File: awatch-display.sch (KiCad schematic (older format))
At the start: 5 parts

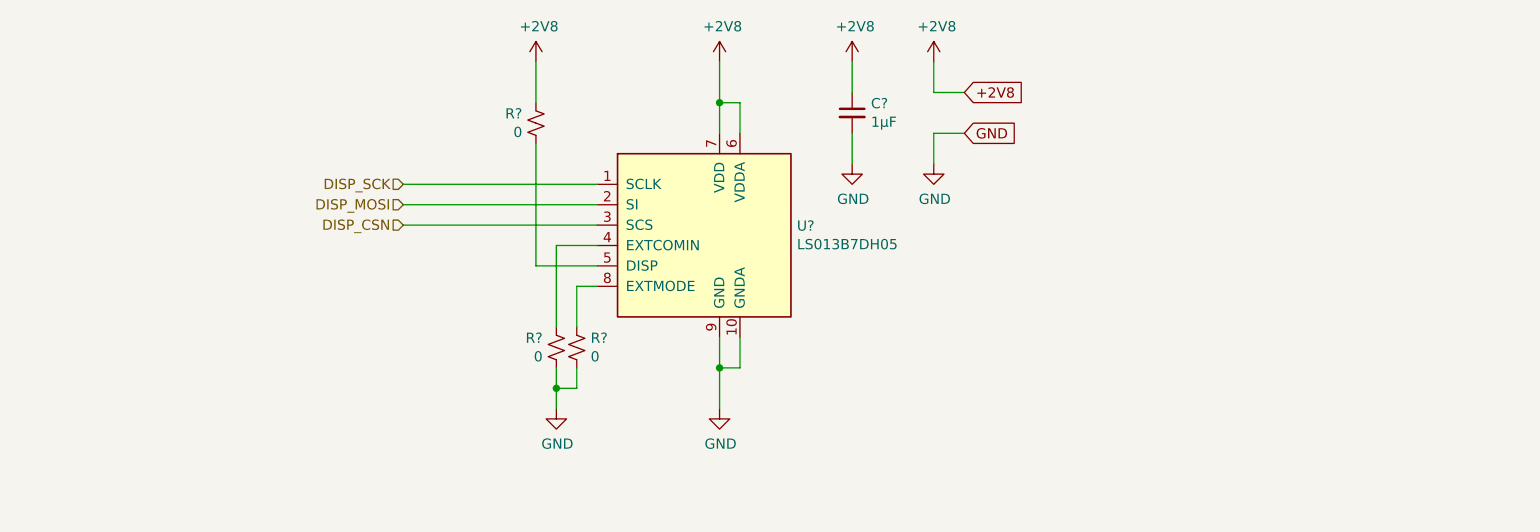
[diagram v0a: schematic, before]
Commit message: backlight PWM through a FET
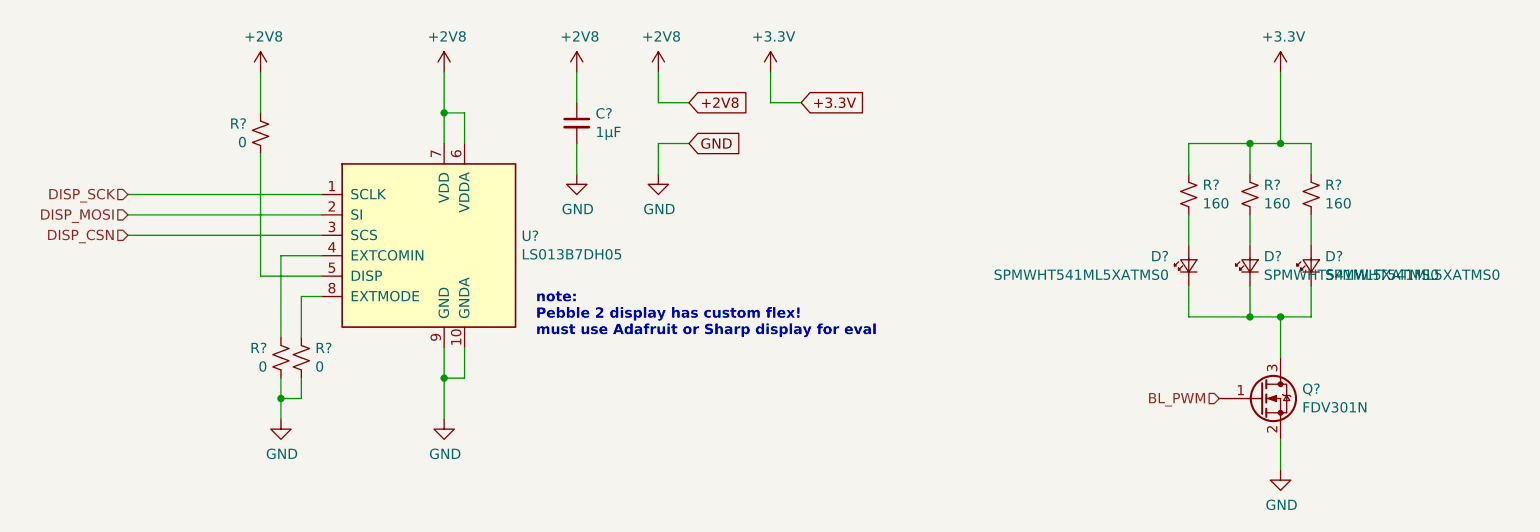
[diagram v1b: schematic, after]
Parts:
- added D? (x3): SPMWHT541ML5XATMS0, symbol Device:LED_Small
- added Q?: FDV301N, Package_TO_SOT_SMD:SOT-23, symbol Transistor_FET:2N7002
- added R? (x3): 160, symbol Device:R_Small_US
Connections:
- net GND: now also Q?.2 (S)
- new net: D?.1 (K), D?.1 (K), D?.1 (K), Q?.3 (D)
- new net: D?.2 (A), R?.2 (x3)
- new net +3V3: R?.1, R?.1, R?.1
- new net BL_PWM: Q?.1 (G)
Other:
- note added: "note:\nPebble 2 display has custom flex!\nmust use Adafruit or Sharp display for eval"
- moved on the sheet: C?, R?, U?

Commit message: annotate all
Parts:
- gave numbers to parts that had none: 12
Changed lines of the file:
@@
 $EndDescr
 $Comp
-L awatch-parts:LS013B7DH05 U?
+L awatch-parts:LS013B7DH05 U701
 U 1 1 5C4574CC
 P 3800 3250
-F 0 "U?" H 4779 2846 50  0000 L CNN
+F 0 "U701" H 4779 2846 50  0000 L CNN
 F 1 "LS013B7DH05" H 4779 2755 50  0000 L CNN
 F 2 "" H 3800 3250 50  0001 C CNN
@@
 	3700 3950 3700 4150
 $Comp
-L Device:R_Small_US R?
+L Device:R_Small_US R703
 U 1 1 5C45C395
 P 3700 4250
-F 0 "R?" H 3768 4296 50  0000 L CNN
+F 0 "R703" H 3768 4296 50  0000 L CNN
 F 1 "0" H 3768 4205 50  0000 L CNN
 F 2 "" H 3700 4250 50  0001 C CNN
@@
 $EndComp
 $Comp
-L Device:R_Small_US R?
+L Device:R_Small_US R702
 U 1 1 5C45C3C8
 P 3600 4250
-F 0 "R?" H 3533 4296 50  0000 R CNN
+F 0 "R702" H 3533 4296 50  0000 R CNN
 F 1 "0" H 3533 4205 50  0000 R CNN
 F 2 "" H 3600 4250 50  0001 C CNN
@@
 $EndComp
 $Comp
-L Device:R_Small_US R?
+L Device:R_Small_US R701
 U 1 1 5C45C419
 P 3500 3150
-F 0 "R?" H 3433 3196 50  0000 R CNN
+F 0 "R701" H 3433 3196 50  0000 R CNN
 F 1 "0" H 3433 3105 50  0000 R CNN
 F 2 "" H 3500 3150 50  0001 C CNN
@@
 DISP_CSN
 $Comp
-L power:GND #PWR?
+L power:GND #PWR0172
 U 1 1 5C45D07D
 P 4400 4550
-F 0 "#PWR?" H 4400 4300 50  0001 C CNN
+F 0 "#PWR0172" H 4400 4300 50  0001 C CNN
 F 1 "GND" H 4405 4377 50  0000 C CNN
 F 2 "" H 4400 4550 50  0001 C CNN
@@
 	4400 4350 4400 4550
 $Comp
-L power:+2V8 #PWR?
+L power:+2V8 #PWR0173
 U 1 1 5C45D26E
 P 4400 2850
-F 0 "#PWR?" H 4400 2700 50  0001 C CNN
+F 0 "#PWR0173" H 4400 2700 50  0001 C CNN
 F 1 "+2V8" H 4415 3023 50  0000 C CNN
 F 2 "" H 4400 2850 50  0001 C CNN
@@
 Connection ~ 4400 3050
 $Comp
-L power:+2V8 #PWR?
+L power:+2V8 #PWR0174
 U 1 1 5C45DE11
 P 3500 2850
-F 0 "#PWR?" H 3500 2700 50  0001 C CNN
+F 0 "#PWR0174" H 3500 2700 50  0001 C CNN
 F 1 "+2V8" H 3515 3023 50  0000 C CNN
 F 2 "" H 3500 2850 50  0001 C CNN
@@
 	3500 2850 3500 3050
 $Comp
-L power:GND #PWR?
+L power:GND #PWR0175
 U 1 1 5C45DF78
 P 3600 4550
-F 0 "#PWR?" H 3600 4300 50  0001 C CNN
+F 0 "#PWR0175" H 3600 4300 50  0001 C CNN
 F 1 "GND" H 3605 4377 50  0000 C CNN
 F 2 "" H 3600 4550 50  0001 C CNN
@@
 	3600 4450 3600 4550
 $Comp
-L Device:C_Small C?
+L Device:C_Small C701
 U 1 1 5C45E33C
 P 5050 3100
-F 0 "C?" H 5142 3146 50  0000 L CNN
+F 0 "C701" H 5142 3146 50  0000 L CNN
 F 1 "1µF" H 5142 3055 50  0000 L CNN
 F 2 "" H 5050 3100 50  0001 C CNN
@@
 $EndComp
 $Comp
-L power:+2V8 #PWR?
+L power:+2V8 #PWR0176
 U 1 1 5C45E392
 P 5050 2850
-F 0 "#PWR?" H 5050 2700 50  0001 C CNN
+F 0 "#PWR0176" H 5050 2700 50  0001 C CNN
 F 1 "+2V8" H 5065 3023 50  0000 C CNN
 F 2 "" H 5050 2850 50  0001 C CNN
@@
 $EndComp
 $Comp
-L power:GND #PWR?
+L power:GND #PWR0177
 U 1 1 5C45E3CA
 P 5050 3350
-F 0 "#PWR?" H 5050 3100 50  0001 C CNN
+F 0 "#PWR0177" H 5050 3100 50  0001 C CNN
 F 1 "GND" H 5055 3177 50  0000 C CNN
 F 2 "" H 5050 3350 50  0001 C CNN
@@
 	5050 3200 5050 3350
 $Comp
-L power:GND #PWR?
+L power:GND #PWR0178
 U 1 1 5C45EF4F
 P 5450 3350
-F 0 "#PWR?" H 5450 3100 50  0001 C CNN
+F 0 "#PWR0178" H 5450 3100 50  0001 C CNN
 F 1 "GND" H 5455 3177 50  0000 C CNN
 F 2 "" H 5450 3350 50  0001 C CNN
@@
 note:\nPebble 2 display has custom flex!\nmust use Adafruit or Sharp display for eval
 $Comp
-L Device:LED_Small D?
+L Device:LED_Small D701
 U 1 1 5C46F2C3
 P 8050 3800
-F 0 "D?" V 8096 3897 50  0000 L CNN
+F 0 "D701" V 8096 3897 50  0000 L CNN
 F 1 "SPMWHT541ML5XATMS0" V 8005 3897 50  0000 L CNN
 F 2 "" V 8050 3800 50  0001 C CNN
@@
 $EndComp
 $Comp
-L Device:LED_Small D?
+L Device:LED_Small D702
 U 1 1 5C46F39B
 P 8350 3800
-F 0 "D?" V 8396 3732 50  0000 R CNN
+F 0 "D702" V 8396 3732 50  0000 R CNN
 F 1 "SPMWHT541ML5XATMS0" V 8305 3732 50  0000 R CNN
 F 2 "" V 8350 3800 50  0001 C CNN
@@
 $EndComp
 $Comp
-L Device:LED_Small D?
+L Device:LED_Small D703
 U 1 1 5C46F3B9
 P 8650 3800
-F 0 "D?" V 8696 3732 50  0000 R CNN
+F 0 "D703" V 8696 3732 50  0000 R CNN
 F 1 "SPMWHT541ML5XATMS0" V 8605 3732 50  0000 R CNN
 F 2 "" V 8650 3800 50  0001 C CNN
@@
 $EndComp
 $Comp
-L Device:R_Small_US R?
+L Device:R_Small_US R704
 U 1 1 5C4700C1
 P 8050 3450
-F 0 "R?" H 8118 3496 50  0000 L CNN
+F 0 "R704" H 8118 3496 50  0000 L CNN
 F 1 "160" H 8118 3405 50  0000 L CNN
 F 2 "" H 8050 3450 50  0001 C CNN
@@
 $EndComp
 $Comp
-L Device:R_Small_US R?
+L Device:R_Small_US R705
 U 1 1 5C47011E
 P 8350 3450
-F 0 "R?" H 8418 3496 50  0000 L CNN
+F 0 "R705" H 8418 3496 50  0000 L CNN
 F 1 "160" H 8418 3405 50  0000 L CNN
 F 2 "" H 8350 3450 50  0001 C CNN
@@
 $EndComp
 $Comp
-L Device:R_Small_US R?
+L Device:R_Small_US R706
 U 1 1 5C470142
 P 8650 3450
-F 0 "R?" H 8718 3496 50  0000 L CNN
+F 0 "R706" H 8718 3496 50  0000 L CNN
 F 1 "160" H 8718 3405 50  0000 L CNN
 F 2 "" H 8650 3450 50  0001 C CNN
@@
 	8500 3200 8650 3200
 $Comp
-L power:+3.3V #PWR?
+L power:+3.3V #PWR0179
 U 1 1 5C473467
 P 8500 2850
-F 0 "#PWR?" H 8500 2700 50  0001 C CNN
+F 0 "#PWR0179" H 8500 2700 50  0001 C CNN
 F 1 "+3.3V" H 8515 3023 50  0000 C CNN
 F 2 "" H 8500 2850 50  0001 C CNN
@@
 	8500 2850 8500 3200
 $Comp
-L power:+2V8 #PWR?
+L power:+2V8 #PWR0180
 U 1 1 5C474266
 P 5450 2850
-F 0 "#PWR?" H 5450 2700 50  0001 C CNN
+F 0 "#PWR0180" H 5450 2700 50  0001 C CNN
 F 1 "+2V8" H 5465 3023 50  0000 C CNN
 F 2 "" H 5450 2850 50  0001 C CNN
@@
 	5450 3000 5450 2850
 $Comp
-L power:+3.3V #PWR?
+L power:+3.3V #PWR0181
 U 1 1 5C4749C5
 P 6000 2850
-F 0 "#PWR?" H 6000 2700 50  0001 C CNN
+F 0 "#PWR0181" H 6000 2700 50  0001 C CNN
 F 1 "+3.3V" H 6015 3023 50  0000 C CNN
 F 2 "" H 6000 2850 50  0001 C CNN
@@
 $EndComp
 $Comp
-L Transistor_FET:2N7002 Q?
+L Transistor_FET:2N7002 Q701
 U 1 1 5C474E7A
 P 8400 4450
-F 0 "Q?" H 8606 4496 50  0000 L CNN
+F 0 "Q701" H 8606 4496 50  0000 L CNN
 F 1 "FDV301N" H 8606 4405 50  0000 L CNN
 F 2 "Package_TO_SOT_SMD:SOT-23" H 8600 4375 50  0001 L CIN
@@
 	8500 4650 8500 4800
 $Comp
-L power:GND #PWR?
+L power:GND #PWR0182
 U 1 1 5C475EE3
 P 8500 4800
-F 0 "#PWR?" H 8500 4550 50  0001 C CNN
+F 0 "#PWR0182" H 8500 4550 50  0001 C CNN
 F 1 "GND" H 8505 4627 50  0000 C CNN
 F 2 "" H 8500 4800 50  0001 C CNN

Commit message: Add footprints.
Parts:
- C701: footprint (none) -> Capacitor_SMD:C_0603_1608Metric
- D701, D702, D703: footprint (none) -> LED_SMD:LED_PLCC_2835_Handsoldering
- R701, R702, R703, R704, R705, R706: footprint (none) -> Resistor_SMD:R_0603_1608Metric
- U701: footprint (none) -> awatch2-footprints:Panasonic_Y5B_AYF531035_1x10-1MP_P0.50mm_Horizontal
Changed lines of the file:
@@
 EESchema Schematic File Version 4
+LIBS:awatch2-cache
 EELAYER 26 0
 EELAYER END
@@
 F 0 "U701" H 4779 2846 50  0000 L CNN
 F 1 "LS013B7DH05" H 4779 2755 50  0000 L CNN
-F 2 "" H 3800 3250 50  0001 C CNN
+F 2 "awatch2-footprints:Panasonic_Y5B_AYF531035_1x10-1MP_P0.50mm_Horizontal" H 3800 3250 50  0001 C CNN
 F 3 "" H 3800 3250 50  0001 C CNN
 	1    3800 3250
@@
 F 0 "R703" H 3768 4296 50  0000 L CNN
 F 1 "0" H 3768 4205 50  0000 L CNN
-F 2 "" H 3700 4250 50  0001 C CNN
+F 2 "Resistor_SMD:R_0603_1608Metric" H 3700 4250 50  0001 C CNN
 F 3 "~" H 3700 4250 50  0001 C CNN
 	1    3700 4250
@@
 F 0 "R702" H 3533 4296 50  0000 R CNN
 F 1 "0" H 3533 4205 50  0000 R CNN
-F 2 "" H 3600 4250 50  0001 C CNN
+F 2 "Resistor_SMD:R_0603_1608Metric" H 3600 4250 50  0001 C CNN
 F 3 "~" H 3600 4250 50  0001 C CNN
 	1    3600 4250
@@
 F 0 "R701" H 3433 3196 50  0000 R CNN
 F 1 "0" H 3433 3105 50  0000 R CNN
-F 2 "" H 3500 3150 50  0001 C CNN
+F 2 "Resistor_SMD:R_0603_1608Metric" H 3500 3150 50  0001 C CNN
 F 3 "~" H 3500 3150 50  0001 C CNN
 	1    3500 3150
@@
 F 0 "C701" H 5142 3146 50  0000 L CNN
 F 1 "1µF" H 5142 3055 50  0000 L CNN
-F 2 "" H 5050 3100 50  0001 C CNN
+F 2 "Capacitor_SMD:C_0603_1608Metric" H 5050 3100 50  0001 C CNN
 F 3 "~" H 5050 3100 50  0001 C CNN
 	1    5050 3100
@@
 F 0 "D701" V 8096 3897 50  0000 L CNN
 F 1 "SPMWHT541ML5XATMS0" V 8005 3897 50  0000 L CNN
-F 2 "" V 8050 3800 50  0001 C CNN
+F 2 "LED_SMD:LED_PLCC_2835_Handsoldering" V 8050 3800 50  0001 C CNN
 F 3 "~" V 8050 3800 50  0001 C CNN
 	1    8050 3800
@@
 F 0 "D702" V 8396 3732 50  0000 R CNN
 F 1 "SPMWHT541ML5XATMS0" V 8305 3732 50  0000 R CNN
-F 2 "" V 8350 3800 50  0001 C CNN
+F 2 "LED_SMD:LED_PLCC_2835_Handsoldering" V 8350 3800 50  0001 C CNN
 F 3 "~" V 8350 3800 50  0001 C CNN
 	1    8350 3800
@@
 F 0 "D703" V 8696 3732 50  0000 R CNN
 F 1 "SPMWHT541ML5XATMS0" V 8605 3732 50  0000 R CNN
-F 2 "" V 8650 3800 50  0001 C CNN
+F 2 "LED_SMD:LED_PLCC_2835_Handsoldering" V 8650 3800 50  0001 C CNN
 F 3 "~" V 8650 3800 50  0001 C CNN
 	1    8650 3800
@@
 F 0 "R704" H 8118 3496 50  0000 L CNN
 F 1 "160" H 8118 3405 50  0000 L CNN
-F 2 "" H 8050 3450 50  0001 C CNN
+F 2 "Resistor_SMD:R_0603_1608Metric" H 8050 3450 50  0001 C CNN
 F 3 "~" H 8050 3450 50  0001 C CNN
 	1    8050 3450
@@
 F 0 "R705" H 8418 3496 50  0000 L CNN
 F 1 "160" H 8418 3405 50  0000 L CNN
-F 2 "" H 8350 3450 50  0001 C CNN
+F 2 "Resistor_SMD:R_0603_1608Metric" H 8350 3450 50  0001 C CNN
 F 3 "~" H 8350 3450 50  0001 C CNN
 	1    8350 3450
@@
 F 0 "R706" H 8718 3496 50  0000 L CNN
 F 1 "160" H 8718 3405 50  0000 L CNN
-F 2 "" H 8650 3450 50  0001 C CNN
+F 2 "Resistor_SMD:R_0603_1608Metric" H 8650 3450 50  0001 C CNN
 F 3 "~" H 8650 3450 50  0001 C CNN
 	1    8650 3450

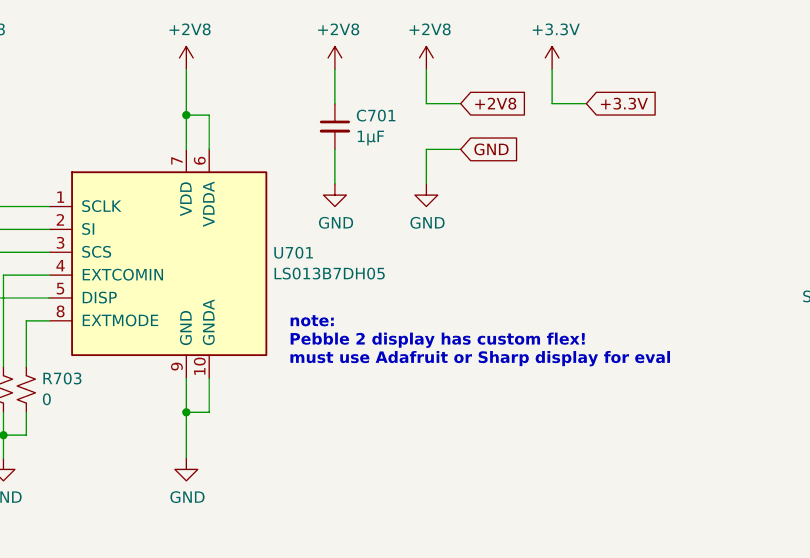
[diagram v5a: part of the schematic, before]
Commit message: add BOM part for connector for display
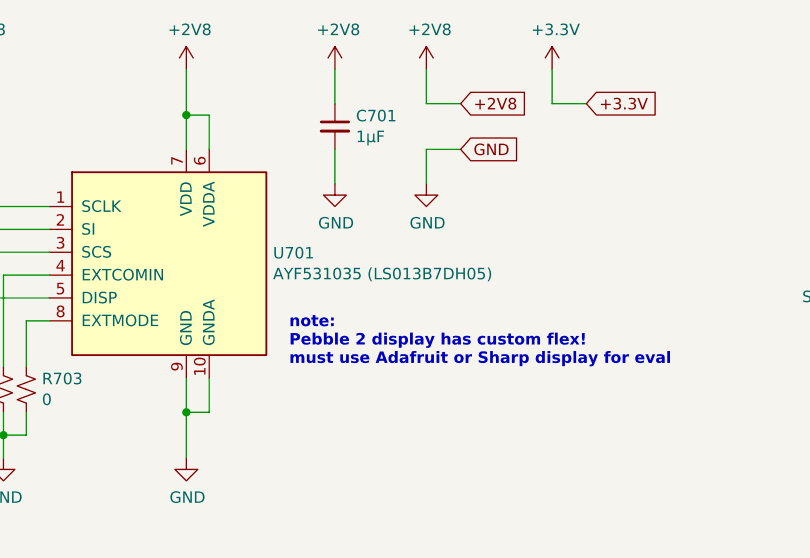
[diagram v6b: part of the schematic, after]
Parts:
- U701: value LS013B7DH05 -> AYF531035 (LS013B7DH05)
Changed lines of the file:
@@
 P 3800 3250
 F 0 "U701" H 4779 2846 50  0000 L CNN
-F 1 "LS013B7DH05" H 4779 2755 50  0000 L CNN
+F 1 "AYF531035 (LS013B7DH05)" H 4779 2755 50  0000 L CNN
 F 2 "awatch2-footprints:Panasonic_Y5B_AYF531035_1x10-1MP_P0.50mm_Horizontal" H 3800 3250 50  0001 C CNN
 F 3 "" H 3800 3250 50  0001 C CNN

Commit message: approx. final layout
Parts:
- C701: value 1µF -> 1.0µF X7R; DigiKey PN (none) -> 1276-1946-1-ND
- D701, D702, D703: DigiKey PN (none) -> 1510-1284-1-ND
- Q701: DigiKey PN (none) -> FDV301NCT-ND
- U701: DigiKey PN (none) -> 255-5667-ND, Adafruit display
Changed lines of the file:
@@
 $Descr A4 11693 8268
 encoding utf-8
-Sheet 7 9
+Sheet 7 10
 Title "AWatch2"
 Date ""
@@
 F 2 "awatch2-footprints:Panasonic_Y5B_AYF531035_1x10-1MP_P0.50mm_Horizontal" H 3800 3250 50  0001 C CNN
 F 3 "" H 3800 3250 50  0001 C CNN
+F 4 "255-5667-ND, Adafruit display" H 0   0   50  0001 C CNN "DigiKey PN"
 	1    3800 3250
 	1    0    0    -1
@@
 P 5050 3100
 F 0 "C701" H 5142 3146 50  0000 L CNN
-F 1 "1µF" H 5142 3055 50  0000 L CNN
+F 1 "1.0µF X7R" H 5142 3055 50  0000 L CNN
 F 2 "Capacitor_SMD:C_0603_1608Metric" H 5050 3100 50  0001 C CNN
 F 3 "~" H 5050 3100 50  0001 C CNN
+F 4 "1276-1946-1-ND" H 0   0   50  0001 C CNN "DigiKey PN"
 	1    5050 3100
 	1    0    0    -1
@@
 F 2 "LED_SMD:LED_PLCC_2835_Handsoldering" V 8050 3800 50  0001 C CNN
 F 3 "~" V 8050 3800 50  0001 C CNN
+F 4 "1510-1284-1-ND" H 0   0   50  0001 C CNN "DigiKey PN"
 	1    8050 3800
 	0    -1   -1   0
@@
 F 2 "LED_SMD:LED_PLCC_2835_Handsoldering" V 8350 3800 50  0001 C CNN
 F 3 "~" V 8350 3800 50  0001 C CNN
+F 4 "1510-1284-1-ND" H 0   0   50  0001 C CNN "DigiKey PN"
 	1    8350 3800
 	0    -1   -1   0
@@
 F 2 "LED_SMD:LED_PLCC_2835_Handsoldering" V 8650 3800 50  0001 C CNN
 F 3 "~" V 8650 3800 50  0001 C CNN
+F 4 "1510-1284-1-ND" H 0   0   50  0001 C CNN "DigiKey PN"
 	1    8650 3800
 	0    -1   -1   0
@@
 F 2 "Package_TO_SOT_SMD:SOT-23" H 8600 4375 50  0001 L CIN
 F 3 "https://www.fairchildsemi.com/datasheets/2N/2N7002.pdf" H 8400 4450 50  0001 L CNN
+F 4 "FDV301NCT-ND" H 0   0   50  0001 C CNN "DigiKey PN"
 	1    8400 4450
 	1    0    0    -1

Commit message: BOM fully populated
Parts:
- R701, R702, R703: DigiKey PN (none) -> MCT0603-0.0-ZZCT-ND
- R704, R705, R706: DigiKey PN (none) -> 749-1765-1-ND
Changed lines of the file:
@@
 F 2 "Resistor_SMD:R_0603_1608Metric" H 3700 4250 50  0001 C CNN
 F 3 "~" H 3700 4250 50  0001 C CNN
+F 4 "MCT0603-0.0-ZZCT-ND" H 0   0   50  0001 C CNN "DigiKey PN"
 	1    3700 4250
 	1    0    0    -1
@@
 F 2 "Resistor_SMD:R_0603_1608Metric" H 3600 4250 50  0001 C CNN
 F 3 "~" H 3600 4250 50  0001 C CNN
+F 4 "MCT0603-0.0-ZZCT-ND" H 0   0   50  0001 C CNN "DigiKey PN"
 	1    3600 4250
 	1    0    0    -1
@@
 F 2 "Resistor_SMD:R_0603_1608Metric" H 3500 3150 50  0001 C CNN
 F 3 "~" H 3500 3150 50  0001 C CNN
+F 4 "MCT0603-0.0-ZZCT-ND" H 0   0   50  0001 C CNN "DigiKey PN"
 	1    3500 3150
 	1    0    0    -1
@@
 F 2 "Resistor_SMD:R_0603_1608Metric" H 8050 3450 50  0001 C CNN
 F 3 "~" H 8050 3450 50  0001 C CNN
+F 4 "749-1765-1-ND" H 0   0   50  0001 C CNN "DigiKey PN"
 	1    8050 3450
 	1    0    0    -1
@@
 F 2 "Resistor_SMD:R_0603_1608Metric" H 8350 3450 50  0001 C CNN
 F 3 "~" H 8350 3450 50  0001 C CNN
+F 4 "749-1765-1-ND" H 0   0   50  0001 C CNN "DigiKey PN"
 	1    8350 3450
 	1    0    0    -1
@@
 F 2 "Resistor_SMD:R_0603_1608Metric" H 8650 3450 50  0001 C CNN
 F 3 "~" H 8650 3450 50  0001 C CNN
+F 4 "749-1765-1-ND" H 0   0   50  0001 C CNN "DigiKey PN"
 	1    8650 3450
 	1    0    0    -1
